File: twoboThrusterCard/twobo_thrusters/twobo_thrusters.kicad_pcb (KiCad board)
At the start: 4 copper layers, 110 x 75 mm, 14 parts, among them J2 Conn_01x09, J5 Conn_02x40_Odd_Even

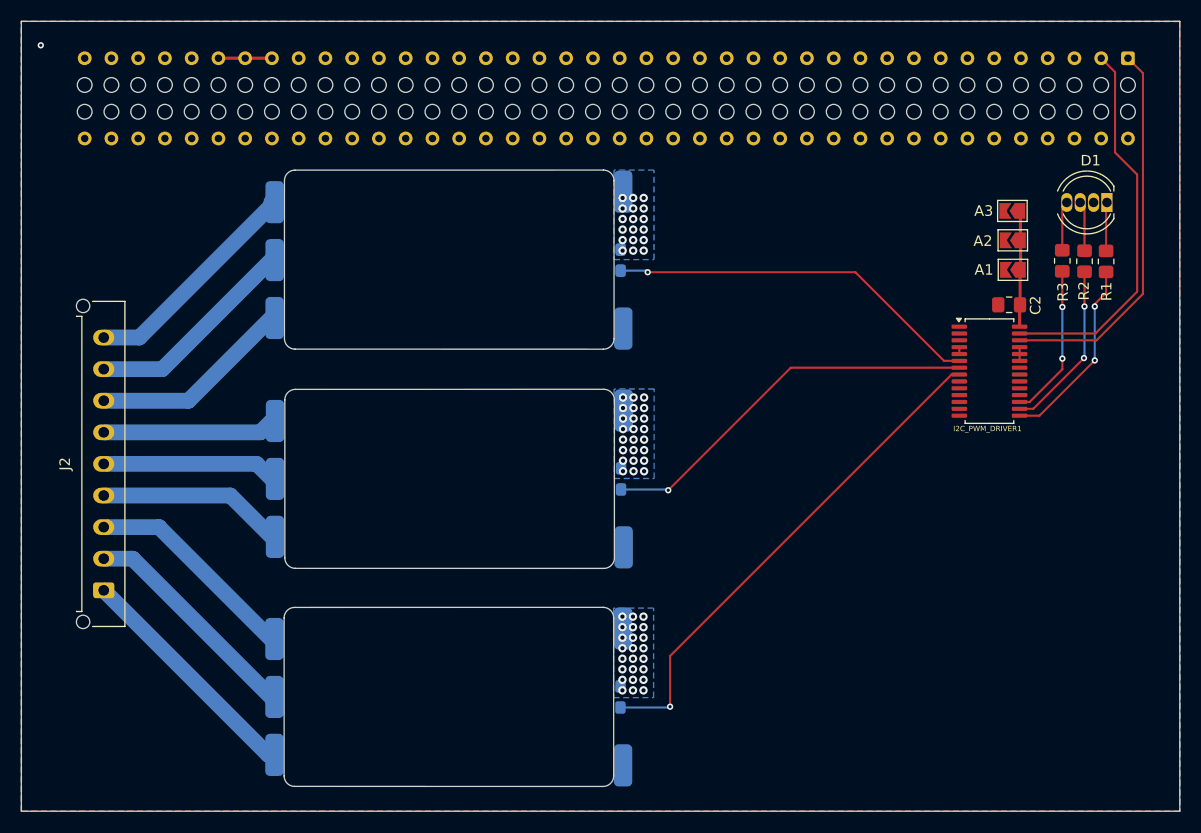
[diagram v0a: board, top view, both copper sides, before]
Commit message: added power routes
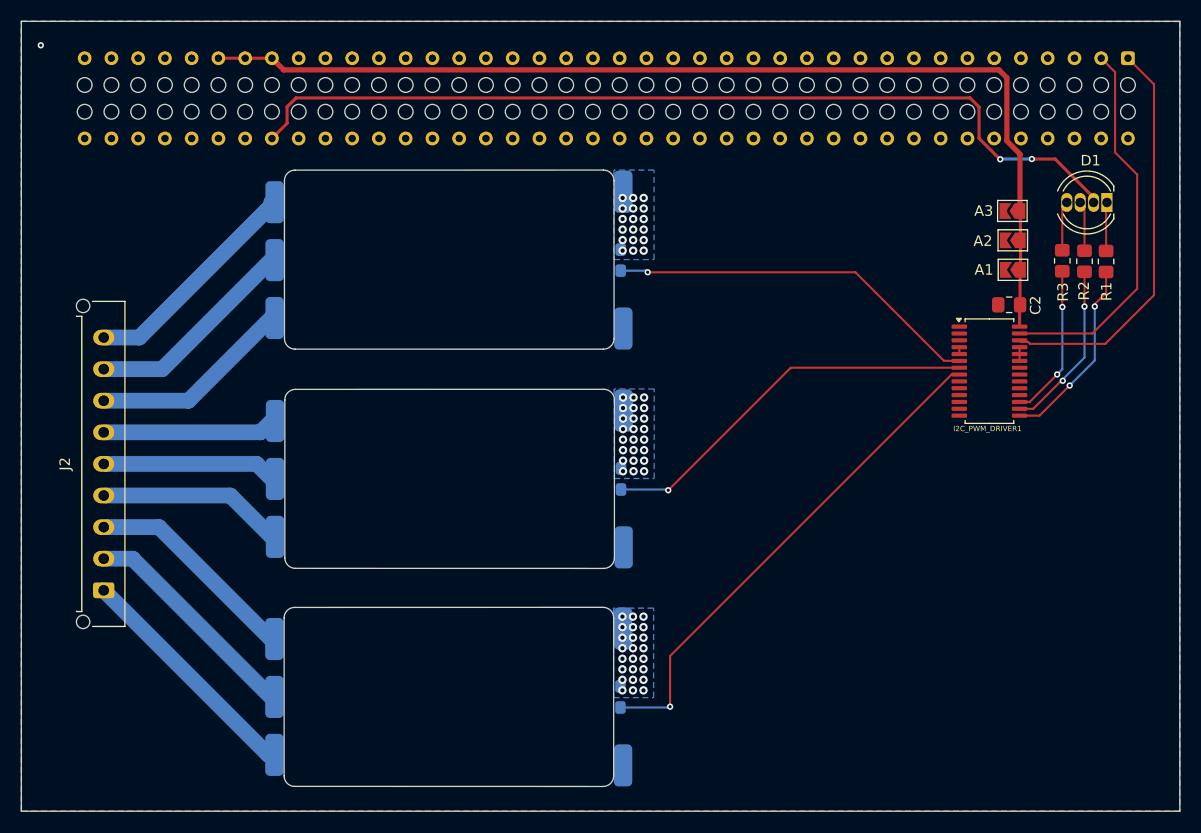
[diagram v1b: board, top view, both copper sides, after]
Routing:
- net +5V: track 0.00 -> 86.7 mm, vias 0 -> 2
- net +3.3V: track 16.1 -> 99.8 mm
- net SCL: track 36.5 -> 38.3 mm
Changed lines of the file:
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@@
+	)
+	(segment
+		(start 151.81 67.2)
+		(end 151.81 66.73)
+		(width 0.3)
+		(layer "F.Cu")
+		(net 2)
+	)
+	(segment
+		(start 151.81 66.73)
+		(end 148.155 63.075)
+		(width 0.3)
+		(layer "F.Cu")
+		(net 2)
+	)
+	(segment
+		(start 142.95 63.1)
+		(end 142.927301 63.1)
+		(width 0.3)
+		(layer "F.Cu")
+		(net 2)
+	)
+	(segment
+		(start 140.936 61.108699)
+		(end 140.936 58.128951)
+		(width 0.3)
+		(layer "F.Cu")
+		(net 2)
+	)
+	(segment
+		(start 140.082049 57.275)
+		(end 76.087951 57.275)
+		(width 0.3)
+		(layer "F.Cu")
+		(net 2)
+	)
+	(segment
+		(start 75.234 59.686)
+		(end 73.795 61.125)
+		(width 0.3)
+		(layer "F.Cu")
+		(net 2)
+	)
+	(segment
+		(start 148.155 63.075)
+		(end 145.95 63.075)
+		(width 0.3)
+		(layer "F.Cu")
+		(net 2)
+	)
+	(segment
+		(start 142.927301 63.1)
+		(end 140.936 61.108699)
+		(width 0.3)
+		(layer "F.Cu")
+		(net 2)
+	)
+	(segment
+		(start 75.234 58.128951)
+		(end 75.234 59.686)
+		(width 0.3)
+		(layer "F.Cu")
+		(net 2)
+	)
+	(segment
+		(start 140.936 58.128951)
+		(end 140.082049 57.275)
+		(width 0.3)
+		(layer "F.Cu")
+		(net 2)
+	)
+	(segment
+		(start 76.087951 57.275)
+		(end 75.234 58.128951)
+		(width 0.3)
+		(layer "F.Cu")
+		(net 2)
+	)
+	(via
+		(at 145.95 63.075)
+		(size 0.6)
+		(drill 0.3)
+		(layers "F.Cu" "B.Cu")
+		(net 2)
+	)
+	(via
+		(at 142.95 63.1)
+		(size 0.6)
+		(drill 0.3)
+		(layers "F.Cu" "B.Cu")
+		(net 2)
+	)
+	(segment
+		(start 145.95 63.075)
+		(end 142.975 63.075)
+		(width 0.3)
+		(layer "B.Cu")
+		(net 2)
+	)
+	(segment
+		(start 142.975 63.075)
+		(end 142.95 63.1)
+		(width 0.3)
+		(layer "B.Cu")
+		(net 2)
 	)
 	(segment
@@
 	)
 	(segment
+		(start 144.825 62.599121)
+		(end 143.576 61.350121)
+		(width 0.5)
+		(layer "F.Cu")
+		(net 14)
+	)
+	(segment
+		(start 143.576 55.353879)
+		(end 142.833121 54.611)
+		(width 0.5)
+		(layer "F.Cu")
+		(net 14)
+	)
+	(segment
+		(start 144.825 68.005)
+		(end 144.825 62.599121)
+		(width 0.5)
+		(layer "F.Cu")
+		(net 14)
+	)
+	(segment
 		(start 144.865 68.045)
 		(end 144.825 68.005)
@@
 	)
 	(segment
+		(start 74.901 54.611)
+		(end 73.795 53.505)
+		(width 0.5)
+		(layer "F.Cu")
+		(net 14)
+	)
+	(segment
+		(start 143.576 61.350121)
+		(end 143.576 55.353879)
+		(width 0.5)
+		(layer "F.Cu")
+		(net 14)
+	)
+	(segment
 		(start 144.88 70.81)
 		(end 144.865 70.795)
@@
 	)
 	(segment
-		(start 156.5 75.875)
-		(end 152.085 80.29)
+		(start 142.833121 54.611)
+		(end 74.901 54.611)
+		(width 0.5)
+		(layer "F.Cu")
+		(net 14)
+	)
+	(segment
+		(start 155.075 53.505)
+		(end 157.55 55.98)
 		(width 0.2)
 		(layer "F.Cu")
@@
 	)
 	(segment
-		(start 155.075 53.505)
-		(end 156.5 54.93)
+		(start 157.55 76)
+		(end 152.925 80.625)
 		(width 0.2)
 		(layer "F.Cu")
@@
 	)
 	(segment
-		(start 156.5 54.93)
-		(end 156.5 75.875)
+		(start 152.925 80.625)
+		(end 145.77987 80.625)
 		(width 0.2)
 		(layer "F.Cu")
@@
 	)
 	(segment
-		(start 152.085 80.29)
+		(start 145.77987 80.625)
+		(end 145.59387 80.439)
+		(width 0.2)
+		(layer "F.Cu")
+		(net 15)
+	)
+	(segment
+		(start 157.55 55.98)
+		(end 157.55 76)
+		(width 0.2)
+		(layer "F.Cu")
+		(net 15)
+	)
+	(segment
+		(start 144.9365 80.439)
 		(end 144.7875 80.29)
+		(width 0.2)
+		(layer "F.Cu")
+		(net 15)
+	)
+	(segment
+		(start 145.59387 80.439)
+		(end 144.9365 80.439)
 		(width 0.2)
 		(layer "F.Cu")
@@
 	)
 	(segment
-		(start 150.9 81.975)
+		(start 148.748082 84.126918)
 		(end 146.085 86.79)
+		(width 0.2)
+		(layer "F.Cu")
+		(net 31)
+	)
+	(segment
+		(start 146.085 86.79)
+		(end 144.7875 86.79)
+		(width 0.2)
+		(layer "F.Cu")
+		(net 31)
+	)
+	(segment
+		(start 148.885367 84.126918)
+		(end 148.748082 84.126918)
 		(width 0.2)
 		(layer "F.Cu")
@@
 		(net 31)
 	)
-	(segment
-		(start 146.085 86.79)
-		(end 144.7875 86.79)
-		(width 0.2)
-		(layer "F.Cu")
-		(net 31)
-	)
-	(via
-		(at 150.9 81.975)
+	(via
+		(at 148.885367 84.126918)
 		(size 0.6)
 		(drill 0.3)
@@
 	)
 	(segment
+		(start 148.885367 83.989633)
+		(end 150.95 81.925)
+		(width 0.2)
+		(layer "B.Cu")
+		(net 31)
+	)
+	(segment
+		(start 148.885367 84.126918)
+		(end 148.885367 83.989633)
+		(width 0.2)
+		(layer "B.Cu")
+		(net 31)
+	)
+	(segment
 		(start 150.95 81.925)
-		(end 150.9 81.975)
+		(end 150.95 77.075)
 		(width 0.2)
 		(layer "B.Cu")
@@
 	)
 	(segment
-		(start 150.95 77.075)
-		(end 150.95 81.925)
-		(width 0.2)
-		(layer "B.Cu")
-		(net 31)
+		(start 148.353935 83.528935)
+		(end 145.74287 86.14)
+		(width 0.2)
+		(layer "F.Cu")
+		(net 32)
+	)
+	(segment
+		(start 148.84 73.74)
+		(end 148.84 77.115)
+		(width 0.2)
+		(layer "F.Cu")
+		(net 32)
 	)
 	(segment
@@
 	)
 	(segment
-		(start 148.84 73.74)
-		(end 148.84 77.115)
-		(width 0.2)
-		(layer "F.Cu")
-		(net 32)
-	)
-	(segment
-		(start 148.85 83.03287)
-		(end 145.74287 86.14)
-		(width 0.2)
-		(layer "F.Cu")
-		(net 32)
-	)
-	(segment
 		(start 148.84 77.115)
 		(end 148.85 77.125)
@@
 		(net 32)
 	)
-	(segment
-		(start 148.85 82.025)
-		(end 148.85 83.03287)
-		(width 0.2)
-		(layer "F.Cu")
-		(net 32)
-	)
-	(via
-		(at 148.85 82.025)
+	(via
+		(at 148.353935 83.528935)
 		(size 0.6)
 		(drill 0.3)
@@
 	(segment
 		(start 148.85 77.125)
-		(end 148.85 82.025)
+		(end 148.85 83.03287)
 		(width 0.2)
 		(layer "B.Cu")
@@
 	)
 	(segment
+		(start 148.85 83.03287)
+		(end 148.353935 83.528935)
+		(width 0.2)
+		(layer "B.Cu")
+		(net 32)
+	)
+	(segment
+		(start 149.543414 84.581866)
+		(end 149.543134 84.581866)
+		(width 0.2)
+		(layer "F.Cu")
+		(net 35)
+	)
+	(segment
 		(start 146.685 87.44)
-		(end 151.925 82.2)
+		(end 144.7875 87.44)
+		(width 0.2)
+		(layer "F.Cu")
+		(net 35)
+	)
+	(segment
+		(start 149.543134 84.581866)
+		(end 146.685 87.44)
 		(width 0.2)
 		(layer "F.Cu")
@@
 	)
 	(segment
-		(start 144.7875 87.44)
-		(end 146.685 87.44)
-		(width 0.2)
-		(layer "F.Cu")
-		(net 35)
-	)
-	(segment
 		(start 153 75.775)
 		(end 153 73.8)
@@
 	)
 	(via
-		(at 151.925 82.2)
+		(at 149.543414 84.581866)
 		(size 0.6)
 		(drill 0.3)
@@
 	)
 	(segment
-		(start 151.925 82.2)
+		(start 151.925 82.20028)
 		(end 151.925 77.075)
 		(width 0.2)
 		(layer "B.Cu")
 		(net 35)
+	)
+	(segment
+		(start 149.543414 84.581866)
+		(end 151.925 82.20028)
+		(width 0.2)
+		(layer "B.Cu")
+		(net 35)
+	)
+	(segment
+		(start 153.85 62.45)
+		(end 153.85 54.82)
+		(width 0.2)
+		(layer "F.Cu")
+		(net 37)
+	)
+	(segment
+		(start 144.7875 79.64)
+		(end 151.697788 79.64)
+		(width 0.2)
+		(layer "F.Cu")
+		(net 37)
+	)
+	(segment
+		(start 155.95 64.55)
+		(end 153.85 62.45)
+		(width 0.2)
+		(layer "F.Cu")
+		(net 37)
+	)
+	(segment
+		(start 155.95 75.387788)
+		(end 155.95 64.55)
+		(width 0.2)
+		(layer "F.Cu")
+		(net 37)
+	)
+	(segment
+		(start 151.697788 79.64)
+		(end 155.95 75.387788)
+		(width 0.2)
+		(layer "F.Cu")
+		(net 37)
 	)
 	(segment
@@
 		(width 0.2)
 		(layer "F.Cu")
-		(net 37)
-	)
-	(segment
-		(start 151.985 79.64)
-		(end 155.95 75.675)
-		(width 0.2)
-		(layer "F.Cu")
-		(net 37)
-	)
-	(segment
-		(start 153.85 62.45)
-		(end 153.85 54.82)
-		(width 0.2)
-		(layer "F.Cu")
-		(net 37)
-	)
-	(segment
-		(start 144.7875 79.64)
-		(end 151.985 79.64)
-		(width 0.2)
-		(layer "F.Cu")
-		(net 37)
-	)
-	(segment
-		(start 155.95 64.55)
-		(end 153.85 62.45)
-		(width 0.2)
-		(layer "F.Cu")
-		(net 37)
-	)
-	(segment
-		(start 155.95 75.675)
-		(end 155.95 64.55)
-		(width 0.2)
-		(layer "F.Cu")
